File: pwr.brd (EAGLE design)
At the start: 146.1 x 62.4 mm, 38 parts, among them Q1 IPD65R600C6, T1 750811647, U1 UCC28700

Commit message: save
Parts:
- moved C_2 14.3 mm to (66.4, 33.2)
- moved R_1 14.3 mm to (64.4, 29.0)
- moved C2 14.3 mm to (68.6, 7.10)
- moved C8 14.3 mm to (46.3, 9.60)
- moved U1 14.3 mm to (46.7, 12.3)
- moved C1 14.3 mm to (54.9, 3.50)
- moved C5 14.3 mm to (68.3, 22.5)
- moved C6 14.3 mm to (68.3, 24.6)
- moved C7 14.3 mm to (29.4, 6.20)
- moved C9 14.3 mm to (43.5, 7.00)
- moved D1 14.3 mm to (67.3, 11.0)
- moved D2 14.3 mm to (42.7, 27.5)
- moved D3 14.3 mm to (15.0, 16.1)
- moved D5 14.3 mm to (39.9, 6.70)
- moved F1 14.3 mm to (12.0, 23.0)
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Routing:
- net N$13: track 0.00 -> 51.5 mm
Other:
- board size 146.1 x 62.4 mm -> 143.1 x 48.4 mm

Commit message: save
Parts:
- C7: value 47µF -> EEU-ED2G470S; device derek:CAPPR7.5-16X25 -> derek:CAPPR7.5-18X20
- moved C7 3.81 mm to (28.5, 9.90)
- moved U$2 1.00 mm to (4.00, 26.0)
- moved U$3 1.00 mm to (4.00, 12.0)
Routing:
- net N$13: track 51.5 -> 0.00 mm
- net N$2: track 10.2 -> 9.19 mm
- net N$11: track 9.19 -> 8.19 mm
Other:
- board size 143.1 x 48.4 mm -> 166.1 x 50.8 mm
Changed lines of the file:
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@@
 <wire x1="102.6" y1="40.5" x2="104.76696875" y2="40.5" width="0.001" layer="150"/>
 <wire x1="104.76696875" y1="40.5" x2="106.6" y2="39.3" width="0.001" layer="150" curve="66.421833"/>
-<wire x1="117.1" y1="14.6" x2="101.1" y2="14.6" width="0.254" layer="150"/>
-<wire x1="101.1" y1="14.6" x2="101.1" y2="-10.4" width="0.254" layer="150"/>
-<wire x1="101.1" y1="-10.4" x2="117.1" y2="-10.4" width="0.254" layer="150"/>
-<wire x1="117.1" y1="-10.4" x2="117.1" y2="-7.6" width="0.254" layer="20"/>
-<wire x1="73.5" y1="38" x2="22" y2="33" width="0.001" layer="20"/>
-<wire x1="73.5" y1="0" x2="22" y2="5" width="0.001" layer="20"/>
-<wire x1="20" y1="31" x2="0" y2="29" width="0.001" layer="20"/>
-<wire x1="0" y1="29" x2="0" y2="9" width="0.001" layer="20"/>
-<wire x1="0" y1="9" x2="20" y2="7" width="0.001" layer="20"/>
-<circle x="109.1" y="-10.4" radius="8" width="0.1524" layer="150"/>
-<wire x1="153.1" y1="14.6" x2="143.1" y2="14.6" width="0.254" layer="150"/>
-<wire x1="143.1" y1="14.6" x2="143.1" y2="-5.4" width="0.254" layer="150"/>
-<wire x1="143.1" y1="-5.4" x2="153.1" y2="-5.4" width="0.254" layer="150"/>
-<wire x1="153.1" y1="-5.4" x2="153.1" y2="14.6" width="0.254" layer="150"/>
-<circle x="148.1" y="-5.4" radius="5" width="0.1524" layer="150"/>
-<wire x1="143.1" y1="14.6" x2="117.1" y2="14.6" width="0.254" layer="150"/>
-<wire x1="117.1" y1="14.6" x2="117.1" y2="-7.6" width="0.254" layer="150"/>
-<wire x1="117.1" y1="-7.6" x2="143.1" y2="-7.6" width="0.254" layer="150"/>
-<wire x1="143.1" y1="-7.6" x2="143.1" y2="-5.4" width="0.254" layer="20"/>
-<wire x1="20" y1="31" x2="22" y2="33" width="0.001" layer="20"/>
-<wire x1="22" y1="5" x2="20" y2="7" width="0.001" layer="20"/>
+<wire x1="142.1" y1="12.2" x2="126.1" y2="12.2" width="0.254" layer="150"/>
+<wire x1="126.1" y1="12.2" x2="126.1" y2="-12.8" width="0.254" layer="150"/>
+<wire x1="126.1" y1="-12.8" x2="142.1" y2="-12.8" width="0.254" layer="150"/>
+<wire x1="142.1" y1="-12.8" x2="142.1" y2="-10" width="0.254" layer="20"/>
+<wire x1="73.5" y1="38" x2="25" y2="33" width="0.001" layer="20"/>
+<wire x1="73.5" y1="0" x2="25" y2="5" width="0.001" layer="20"/>
+<wire x1="23" y1="31" x2="2" y2="28" width="0.001" layer="20"/>
+<wire x1="2" y1="28" x2="2" y2="10" width="0.001" layer="20"/>
+<wire x1="2" y1="10" x2="23" y2="7" width="0.001" layer="20"/>
+<circle x="134.1" y="-12.8" radius="8" width="0.1524" layer="150"/>
+<wire x1="178.1" y1="12.2" x2="168.1" y2="12.2" width="0.254" layer="150"/>
+<wire x1="168.1" y1="12.2" x2="168.1" y2="-7.8" width="0.254" layer="150"/>
+<wire x1="168.1" y1="-7.8" x2="178.1" y2="-7.8" width="0.254" layer="150"/>
+<wire x1="178.1" y1="-7.8" x2="178.1" y2="12.2" width="0.254" layer="150"/>
+<circle x="173.1" y="-7.8" radius="5" width="0.1524" layer="150"/>
+<wire x1="168.1" y1="12.2" x2="142.1" y2="12.2" width="0.254" layer="150"/>
+<wire x1="142.1" y1="12.2" x2="142.1" y2="-10" width="0.254" layer="150"/>
+<wire x1="142.1" y1="-10" x2="168.1" y2="-10" width="0.254" layer="150"/>
+<wire x1="168.1" y1="-10" x2="168.1" y2="-7.8" width="0.254" layer="20"/>
+<wire x1="23" y1="31" x2="25" y2="33" width="0.001" layer="20"/>
+<wire x1="25" y1="5" x2="23" y2="7" width="0.001" layer="20"/>
 <wire x1="73.5" y1="38" x2="73.5" y2="0" width="0.001" layer="20"/>
+<circle x="218.6" y="0" radius="16" width="0.1524" layer="51"/>
+<polygon width="0.0001" layer="51">
+<vertex x="211.6" y="-12.5"/>
+<vertex x="211.6" y="12.5"/>
+<vertex x="227.6" y="12.5"/>
+<vertex x="227.6" y="-12.5"/>
+</polygon>
+<polygon width="0.1524" layer="51">
+<vertex x="210" y="13"/>
+<vertex x="210" y="-13"/>
+<vertex x="211.6" y="-13"/>
+<vertex x="211.6" y="13"/>
+</polygon>
+<polygon width="0.1524" layer="51">
+<vertex x="231.4" y="8.9"/>
+<vertex x="228.6" y="8.9"/>
+<vertex x="228.6" y="-9.1"/>
+<vertex x="231.4" y="-9.1"/>
+</polygon>
+<polygon width="0.1524" layer="51">
+<vertex x="231.4" y="10"/>
+<vertex x="231.4" y="-10"/>
+<vertex x="233" y="-10"/>
+<vertex x="233" y="10"/>
+</polygon>
+<circle x="218.6" y="0" radius="20" width="0.1524" layer="51"/>
+<circle x="263.6" y="0" radius="16" width="0.1524" layer="51"/>
+<polygon width="0.0001" layer="51">
+<vertex x="256.6" y="-10"/>
+<vertex x="256.6" y="10"/>
+<vertex x="272.6" y="10"/>
+<vertex x="272.6" y="-10"/>
+</polygon>
+<polygon width="0.1524" layer="51">
+<vertex x="255" y="11"/>
+<vertex x="255" y="-11"/>
+<vertex x="256.6" y="-11"/>
+<vertex x="256.6" y="11"/>
+</polygon>
+<polygon width="0.1524" layer="51">
+<vertex x="276.4" y="8.9"/>
+<vertex x="273.6" y="8.9"/>
+<vertex x="273.6" y="-9.1"/>
+<vertex x="276.4" y="-9.1"/>
+</polygon>
+<polygon width="0.1524" layer="51">
+<vertex x="276.4" y="10"/>
+<vertex x="276.4" y="-10"/>
+<vertex x="278" y="-10"/>
+<vertex x="278" y="10"/>
+</polygon>
+<circle x="263.6" y="0" radius="20" width="0.1524" layer="51"/>
+<wire x1="22.48883125" y1="31.849509375" x2="73.48883125" y2="36.46306875" width="0.001" layer="20"/>
+<wire x1="73.48883125" y1="1.4409" x2="22.48883125" y2="6.05445" width="0.001" layer="20"/>
+<wire x1="22.48883125" y1="6.05445" x2="17.48883125" y2="13.70598125" width="0.001" layer="20"/>
+<wire x1="22.48883125" y1="31.849509375" x2="17.48883125" y2="23.69798125" width="0.001" layer="20"/>
+<wire x1="17.48883125" y1="23.69798125" x2="2.48883125" y2="20.691959375" width="0.001" layer="20"/>
+<wire x1="2.48883125" y1="20.691959375" x2="2.48883125" y2="16.712009375" width="0.001" layer="20"/>
+<wire x1="17.48883125" y1="13.70598125" x2="2.48883125" y2="16.712009375" width="0.001" layer="20"/>
+<wire x1="37.48883125" y1="11.20198125" x2="37.48883125" y2="31.20198125" width="0.001" layer="51"/>
+<wire x1="37.48883125" y1="11.20198125" x2="19.48883125" y2="11.20198125" width="0.001" layer="51"/>
+<wire x1="19.48883125" y1="11.20198125" x2="19.48883125" y2="31.20198125" width="0.001" layer="51"/>
+<wire x1="19.48883125" y1="31.20198125" x2="37.48883125" y2="31.20198125" width="0.001" layer="51"/>
+<wire x1="73.48883125" y1="1.4409" x2="73.48883125" y2="36.46306875" width="0.001" layer="20"/>
 </plain>
 <attributes>
@@
 <attribute name="PART_NUMBER" value="RH06-T" x="15" y="16.1" size="1.778" layer="28" rot="MR270" display="off"/>
 </element>
-<element name="U$2" library="derek" package="TP-1502" value="TP-1502" x="3" y="26" rot="R270"/>
-<element name="U$3" library="derek" package="TP-1502" value="TP-1502" x="3" y="12" rot="R270"/>
-<element name="C7" library="derek" package="CAPPR7.5-16X25" value="47µF" x="29.4" y="6.2">
-<attribute name="DATASHEET_URL" value="https://industrial.panasonic.com/cdbs/www-data/pdf/RDF0000/ABA0000C1062.pdf" x="29.4" y="6.2" size="1.778" layer="27" display="off"/>
-<attribute name="DIGIKEY_PART_NUMBER" value="P13545-ND" x="29.4" y="6.2" size="1.778" layer="27" display="off"/>
-<attribute name="MANUFACTURER" value="Panasonic Electronic Components" x="29.4" y="6.2" size="1.778" layer="27" display="off"/>
-<attribute name="PART_NUMBER" value="EEU-ED2G470" x="29.4" y="6.2" size="1.778" layer="27" display="off"/>
-<attribute name="VALUE" value="47µF" x="29.4" y="6.2" size="1.778" layer="27" display="off"/>
-</element>
+<element name="U$2" library="derek" package="TP-1502" value="TP-1502" x="4" y="26" rot="R270"/>
+<element name="U$3" library="derek" package="TP-1502" value="TP-1502" x="4" y="12" rot="R270"/>
+<element name="C7" library="derek" package="CAPPR7.5-18X20" value="EEU-ED2G470S" x="28.5" y="9.9"/>
 <element name="U$9" library="derek" package="TP-1502" value="TP-1502" x="71" y="30"/>
 <element name="U$10" library="derek" package="TP-1502" value="TP-1502" x="71" y="32"/>
@@
 <vertex x="44.8" y="16.6"/>
 </polygon>
+<wire x1="43.5" y1="5.6" x2="49.9" y2="3.5" width="0" layer="19" extent="16-16"/>
+<wire x1="17.95" y1="14.75" x2="32.25" y2="9.9" width="0" layer="19" extent="16-16"/>
 </signal>
 <signal name="N$2">
 <contactref element="U$3" pad="1"/>
 <contactref element="D3" pad="3"/>
-<wire x1="3" y1="12" x2="9.3" y2="12" width="1.27" layer="16"/>
+<wire x1="4" y1="12" x2="9.3" y2="12" width="1.27" layer="16"/>
 <wire x1="9.3" y1="12" x2="12.05" y2="14.75" width="1.27" layer="16"/>
 </signal>
@@
 </polygon>
 <polygon width="0.4064" layer="1" thermals="no">
-<vertex x="27" y="2.8"/>
+<vertex x="27" y="4.8"/>
 <vertex x="27" y="29.9"/>
 <vertex x="39.5" y="29.9"/>
@@
 <vertex x="41.5" y="23.8"/>
 <vertex x="41.5" y="32"/>
-<vertex x="23" y="32"/>
-<vertex x="23" y="17.9"/>
+<vertex x="24" y="32"/>
+<vertex x="24" y="17.9"/>
 <vertex x="17.5" y="17.9"/>
 <vertex x="17.5" y="16.9"/>
-<vertex x="23" y="16.9"/>
-<vertex x="23" y="2.8"/>
+<vertex x="24" y="16.9"/>
+<vertex x="24" y="4.8"/>
 </polygon>
 <via x="40.1" y="27.9" extent="1-16" drill="0.35"/>
@@
 <contactref element="U$2" pad="1"/>
 <contactref element="F1" pad="1"/>
-<wire x1="3" y1="26" x2="11.54" y2="26" width="1.27" layer="16"/>
+<wire x1="4" y1="26" x2="11.54" y2="26" width="1.27" layer="16"/>
 <wire x1="11.54" y1="26" x2="12" y2="25.54" width="1.27" layer="16"/>
 </signal>
-<signal name="N$13">
-<wire x1="22" y1="33" x2="73.5" y2="33" width="0.1524" layer="1"/>
-</signal>
 </signals>

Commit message: saveeee
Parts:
- moved C7 7.90 mm to (28.5, 17.8)
- moved U$2 6.64 mm to (8.00, 20.7)
- moved U$3 6.17 mm to (8.00, 16.7)
- moved D3 5.10 mm to (20.1, 16.2)
- moved F1 4.60 mm to (14.6, 19.2), turned to 180 degrees
- moved C1 1.90 mm to (55.0, 5.40)
- moved Q1 1.81 mm to (33.6, 24.7)
- moved L_1 1.70 mm to (60.9, 31.4)
- moved R10 1.43 mm to (31.0, 15.7)
- moved R9 1.43 mm to (31.0, 13.6)
- moved C2 1.00 mm to (68.5, 8.10)
- moved C4 1.00 mm to (68.3, 21.3)
- moved C5 1.00 mm to (68.3, 23.5)
- moved C6 1.00 mm to (68.3, 25.6)
- moved C8 1.00 mm to (46.3, 10.6)
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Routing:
- net N$11: track 8.19 -> 4.68 mm
- net N$1: track 3.03 -> 1.65 mm
- net 3.3V: track 22.5 -> 21.4 mm
- net N$12: track 14.0 -> 14.8 mm
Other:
- board size 166.1 x 50.8 mm -> 73 x 93.4 mm

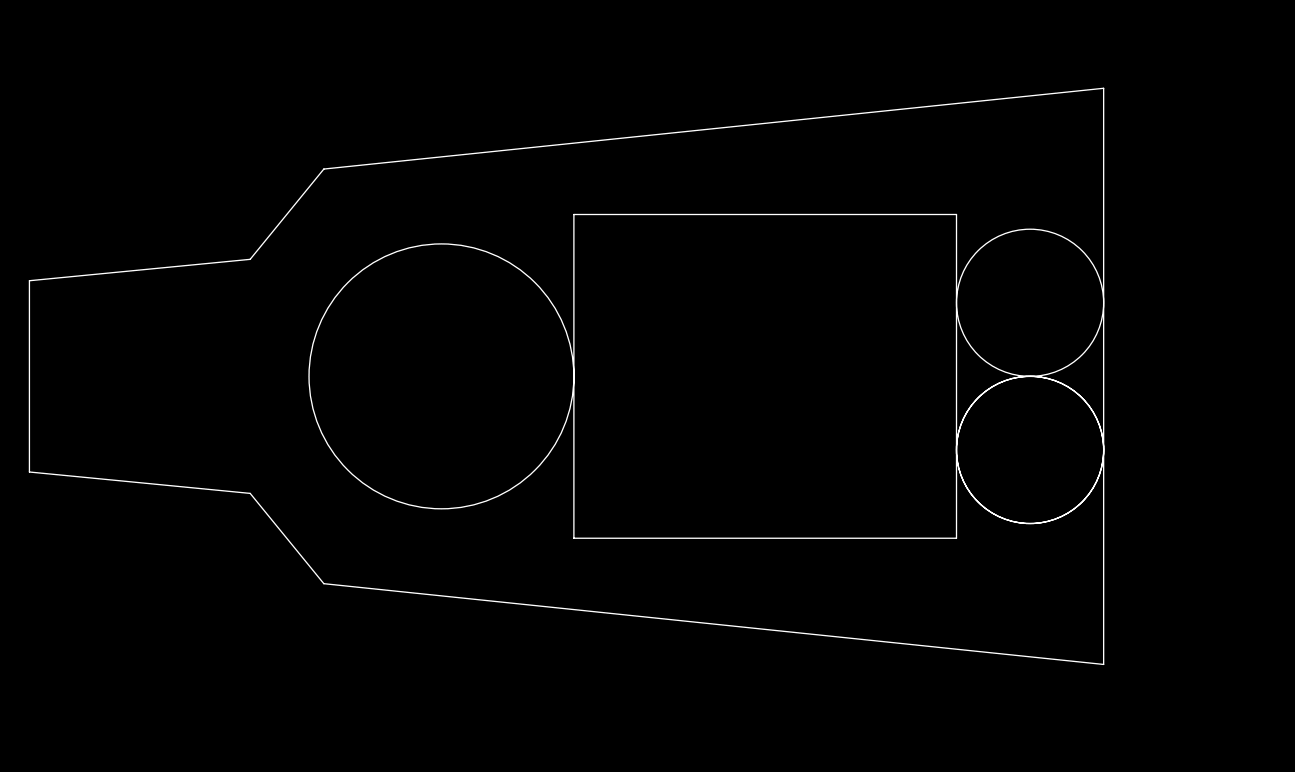
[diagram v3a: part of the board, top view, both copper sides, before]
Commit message: rearrange positions
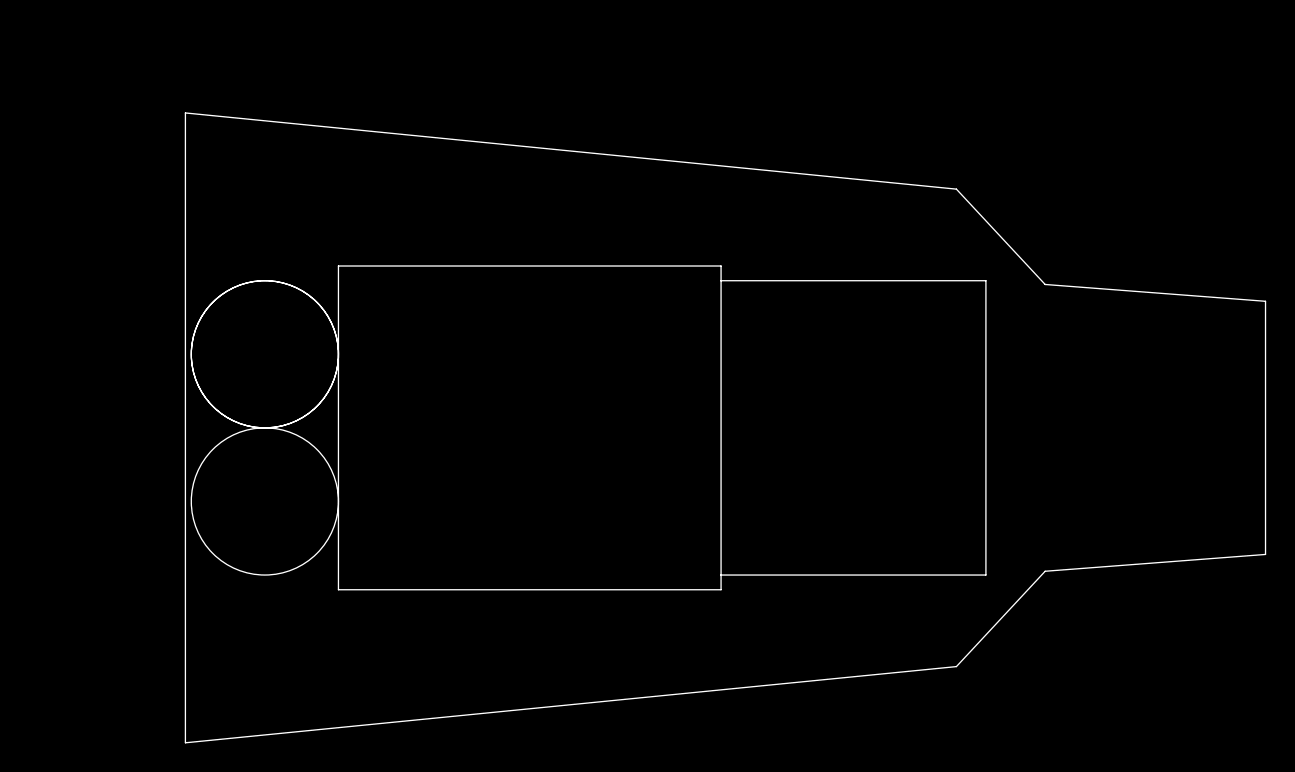
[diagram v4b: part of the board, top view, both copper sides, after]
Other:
- board size 73 x 93.4 mm -> 82.9 x 98.8 mm
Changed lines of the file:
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@@
 <wire x1="17.48883125" y1="23.69798125" x2="22.48883125" y2="31.349509375" width="0.001" layer="20"/>
 <wire x1="22.48883125" y1="31.349509375" x2="73.48883125" y2="35.96306875" width="0.001" layer="20"/>
-<circle x="69.4" y="-42.9" radius="5" width="0" layer="20"/>
-<circle x="69.4" y="-32.9" radius="5" width="0" layer="20"/>
-<circle x="29.4" y="-37.9" radius="9" width="0" layer="20"/>
-<circle x="69.4" y="-42.9" radius="5" width="0" layer="20"/>
-<wire x1="64.4" y1="-48.9" x2="64.4" y2="-26.9" width="0" layer="20"/>
-<wire x1="64.4" y1="-26.9" x2="38.4" y2="-26.9" width="0" layer="20"/>
-<wire x1="38.4" y1="-26.9" x2="38.4" y2="-48.9" width="0" layer="20"/>
-<wire x1="38.4" y1="-48.9" x2="64.4" y2="-48.9" width="0" layer="20"/>
-<wire x1="74.4" y1="-18.32348125" x2="21.407459375" y2="-23.81175" width="0" layer="20"/>
-<wire x1="21.407459375" y1="-23.81175" x2="16.4" y2="-29.947640625" width="0" layer="20"/>
-<wire x1="16.4" y1="-29.947640625" x2="1.4" y2="-31.40076875" width="0" layer="20"/>
-<wire x1="1.4" y1="-31.40076875" x2="1.4" y2="-44.39923125" width="0" layer="20"/>
-<wire x1="1.4" y1="-44.39923125" x2="16.4" y2="-45.852359375" width="0" layer="20"/>
-<wire x1="16.4" y1="-45.852359375" x2="21.407459375" y2="-51.98825" width="0" layer="20"/>
-<wire x1="21.407459375" y1="-51.98825" x2="74.4" y2="-57.47651875" width="0" layer="20"/>
-<wire x1="74.4" y1="-57.47651875" x2="74.4" y2="-18.32348125" width="0" layer="20"/>
+<circle x="17.4" y="-36.4" radius="5" width="0" layer="20"/>
+<circle x="17.4" y="-46.4" radius="5" width="0" layer="20"/>
+<circle x="17.4" y="-36.4" radius="5" width="0" layer="20"/>
+<wire x1="22.4" y1="-30.4" x2="22.4" y2="-52.4" width="0" layer="20"/>
+<wire x1="22.4" y1="-52.4" x2="48.4" y2="-52.4" width="0" layer="20"/>
+<wire x1="48.4" y1="-52.4" x2="48.4" y2="-51.4" width="0" layer="20"/>
+<wire x1="48.4" y1="-31.4" x2="48.4" y2="-30.4" width="0" layer="20"/>
+<wire x1="48.4" y1="-30.4" x2="22.4" y2="-30.4" width="0" layer="20"/>
+<wire x1="12" y1="-62.8007" x2="64.394159375" y2="-57.62306875" width="0" layer="20"/>
+<wire x1="64.394159375" y1="-57.62306875" x2="70.42495" y2="-51.1444" width="0" layer="20"/>
+<wire x1="70.42495" y1="-51.1444" x2="85.4" y2="-50.001740625" width="0" layer="20"/>
+<wire x1="85.4" y1="-50.001740625" x2="85.4" y2="-32.798259375" width="0" layer="20"/>
+<wire x1="85.4" y1="-32.798259375" x2="70.42495" y2="-31.6556" width="0" layer="20"/>
+<wire x1="70.42495" y1="-31.6556" x2="64.394159375" y2="-25.17693125" width="0" layer="20"/>
+<wire x1="64.394159375" y1="-25.17693125" x2="12" y2="-19.9993" width="0" layer="20"/>
+<wire x1="12" y1="-19.9993" x2="12" y2="-62.8007" width="0" layer="20"/>
+<wire x1="66.4" y1="-51.4" x2="48.4" y2="-51.4" width="0" layer="20"/>
+<wire x1="48.4" y1="-51.4" x2="48.4" y2="-31.4" width="0" layer="20"/>
+<wire x1="48.4" y1="-31.4" x2="66.4" y2="-31.4" width="0" layer="20"/>
+<wire x1="66.4" y1="-31.4" x2="66.4" y2="-51.4" width="0" layer="20"/>
 </plain>
 <attributes>

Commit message: ORDERED
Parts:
- removed C_1: 2.2µF, derek:0603
- removed C_2: 22µF, derek:0805
- removed L_1: 10µH, derek:SDR0503
- removed R101: 10k, derek:1206
- removed R_1: 100k, derek:0402
- removed U$10, U$2, U$3, U$8, U$9: TP-1502, derek:TP-1502
- removed U_1: TPS62177, derek:P-WSON(10)
- added 24V, 3.3V, GND, L, N: TP-1502, derek:TP-1502
- added C10: 2.2µF, derek:0603
- added C11: 22µF, derek:0805
- added C3: EEU-ED2G470S, derek:CAPPR7.5-18X20
- added L1: 10µH, derek:SDR0503
- added R12: 100k, derek:0402
- added R7: 33.2, derek:1210
- added U2: TPS62177, derek:P-WSON(10)
- C1: value 2200pF -> 0.1µF; device derek:DE1E3KX222MA4BL01 -> derek:0603
- C2: value 470µF -> 2.2µF; device derek:CAPPR5-10X20 -> derek:1206
- C4: value 4.7µF -> 2200pF; device derek:1206 -> derek:DE1E3KX222MA4BL01
- C6: value 0.1µF -> 4.7µF; device derek:0805 -> derek:1206
- C7: value EEU-ED2G470S -> 220µF; device derek:CAPPR7.5-18X20 -> derek:CAPPR5-10X16
- C8: value 0.1µF -> 220µF; device derek:0603 -> derek:CAPPR5-10X16
- C9: value 2.2µF -> 0.1µF; device derek:1206 -> derek:0805
- D1: value SK4200L-TP -> BAS20HT1G; device derek:SMC -> derek:SOD-323
- D2: value SMAJ120A -> RH06-T; device derek:SMA -> derek:MINIDIP
- D3: value RH06-T -> SMAJ120A; device derek:MINIDIP -> derek:SMA
- D5: value BAS20HT1G -> SK4200L-TP; device derek:SOD-323 -> derek:SMC
- R1: value 10k -> 75k; device derek:1206 -> derek:0603
- R10: value 0.75 -> 10k
- R11: value 19.6k -> 10k; device derek:0603 -> derek:1206
- R2: value 33.2 -> 19.6k; device derek:1210 -> derek:0603
- R4: value 75k -> 698; device derek:0603 -> derek:1206
- R8: value 698 -> 0.75
- moved C6 63.8 mm to (5.20, 16.1), turned to 180 degrees
- moved C5 63.3 mm to (5.20, 18.2), turned to 180 degrees
- moved F1 52.4 mm to (67.0, 21.0), flipped to the top
- moved C4 51.5 mm to (18.5, 34.5), flipped to the top
- moved R11 50.7 mm to (5.20, 36.7), turned to 180 degrees
- moved R1 46.3 mm to (23.8, 29.6)
- moved C2 44.9 mm to (30.0, 31.3), flipped to the bottom, turned to 90 degrees
- moved C8 42.9 mm to (5.00, 22.2), flipped to the top, turned to 0 degrees
- moved C9 40.3 mm to (5.10, 20.1), turned to 180 degrees
- moved D1 40.1 mm to (32.5, 31.9), turned to 90 degrees
- moved D5 39.0 mm to (6.20, 27.3), turned to 180 degrees
- moved C1 36.3 mm to (27.2, 28.7), flipped to the bottom, turned to 0 degrees
- moved R10 32.0 mm to (5.20, 34.6)
- moved R5 27.8 mm to (23.5, 23.8), turned to 90 degrees
- moved C7 27.7 mm to (5.00, 32.4)
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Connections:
- net 24V: now also 24V.1, C10.1, C7.P$1, C8.P$1, C9.1, D5.C, R10.1, R11.1, U2.2, U2.3; no longer C2.P$1, C4.1, C_1.1, D1.C, R1.1, R101.1, U$9.1, U_1.2, U_1.3
- net 3.3V: now also 3.3V.1, C11.1, L1.2, R12.1, U2.10, U2.8; no longer C_2.1, L_1.2, R_1.1, U$8.1, U_1.10, U_1.8
- net GND: now also C2.2, C3.P$2, C4.2, D2.2, R2.2, R8.2; no longer C7.P$2, C8.2, C9.2, D3.2, R10.2, R11.2
- net GND-ISO: now also C10.2, C11.2, C4.1, C7.P$2, C8.P$2, C9.2, GND.1, R10.2, R11.2, U2.1, U2.4, U2.5, U2.6, U2.GND, U2.P$1, U2.P$10, U2.P$2; no longer C1.1, C2.P$2, C4.2, C_1.2, C_2.2, R1.2, R101.2, U$10.1, U_1.1, U_1.4, U_1.5, U_1.6, U_1.GND, U_1.P$1, U_1.P$10, U_1.P$2
- net N$1: now also D2.4; no longer D3.4
- net N$10: now also R7.1; no longer R2.1
- net N$11: now also L.1; no longer U$2.1
- net N$14: now also C1.1, C2.1, D1.C; no longer C8.1, C9.1, D5.C
- net N$15: now also R4.1; no longer R10.1
- net N$16: now also D1.A; no longer D5.A
- net N$17: now also R1.1; no longer R4.1
- net N$18: now also R4.2; no longer R8.2
- net N$2: now also D2.3, N.1; no longer D3.3, U$3.1
- net N$20: now also R1.2, R2.1; no longer R11.1, R4.2
- net N$3: now also C3.P$1, D2.1, D3.A; no longer C7.P$1, D2.A, D3.1
- net N$4: now also R12.2, U2.7; no longer R_1.2, U_1.7
- net N$5: now also L1.1, U2.9; no longer L_1.1, U_1.9
- net N$6: now also D5.A; no longer D1.A
- net N$8: now also D3.C; no longer D2.C
- net N$9: now also R7.2; no longer R2.2
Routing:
- net N$17: track 13.5 -> 21.0 mm
- net 24V: track 0.00 -> 5.07 mm
- net 3.3V: track 21.4 -> 23.9 mm
- net N$1: track 1.65 -> 4.07 mm
- net N$11: track 4.68 -> 6.22 mm
- net N$13: track 14.8 -> 14.0 mm
- net N$16: track 2.94 -> 2.30 mm
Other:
- board size 82.9 x 98.8 mm -> 71 x 42 mm
